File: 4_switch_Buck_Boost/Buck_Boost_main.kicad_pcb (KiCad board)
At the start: 4 copper layers, 96 parts, among them J1 Conn_02x02_Counter_Clockwise, J2 Screw_Terminal_2x5.08, J3 Screw_Terminal_2x2.54, J4 Screw_Terminal_2x5.08, Q101 2N7002K, Q102 NVMFS6H836NLT1G, Q103 BSS83P, Q104 BSC070N10LS5, Q105 BSC070N10LS5, Q106 BSC070N10LS5, Q107 BSC070N10LS5, U1 LT8390EUFD_PBF, U101 LTC4372CMS8-PBF

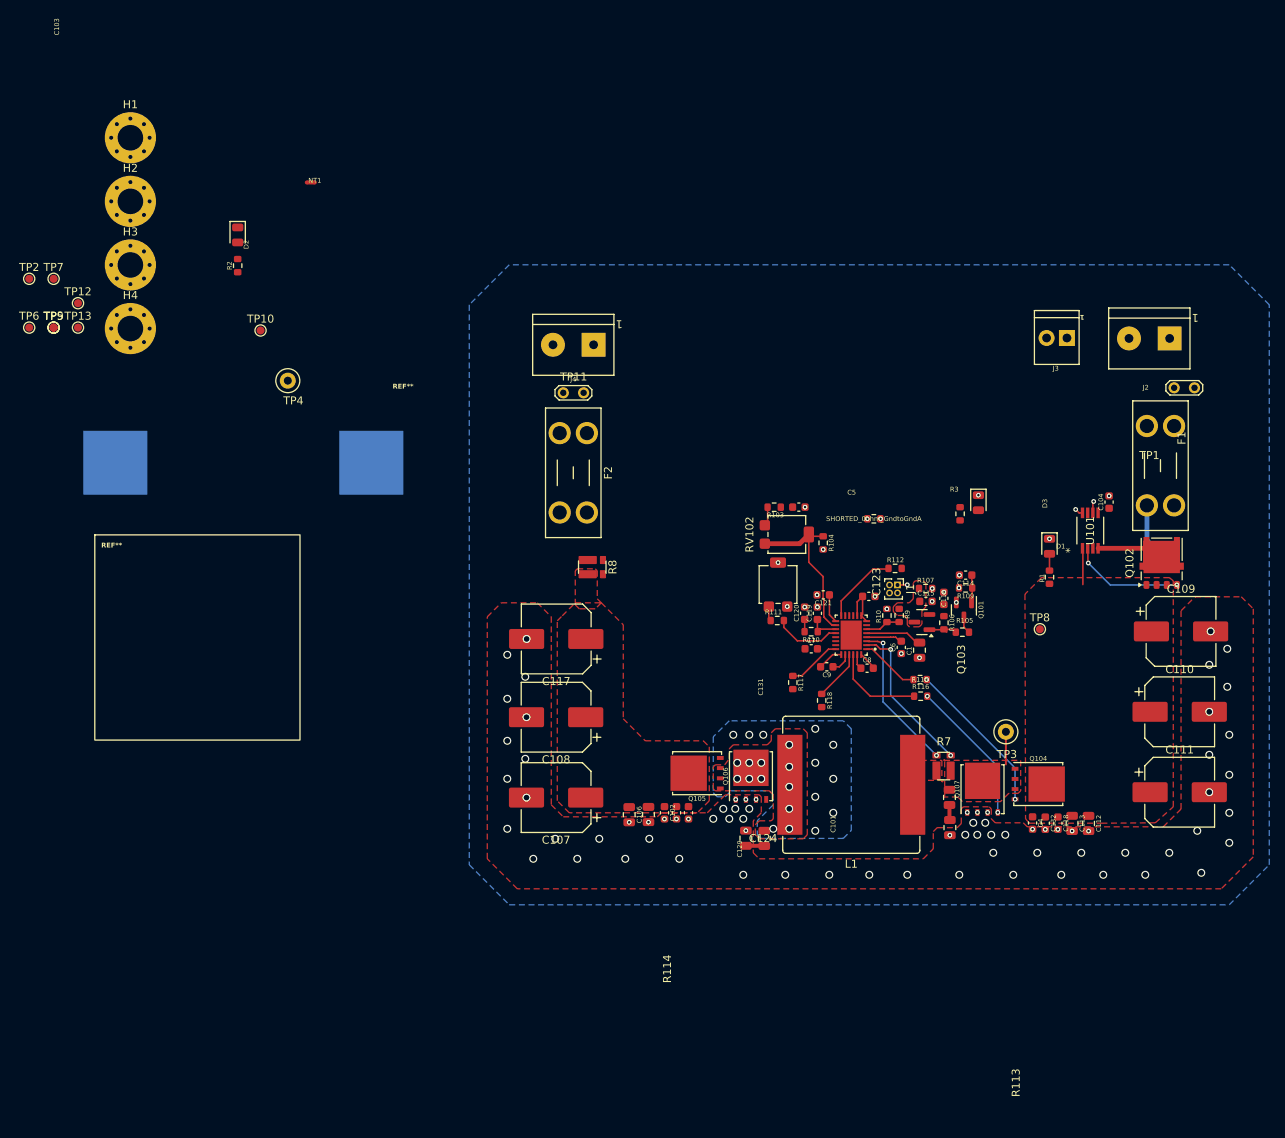
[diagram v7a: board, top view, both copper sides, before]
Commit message: Configured LED, pores, and all test points
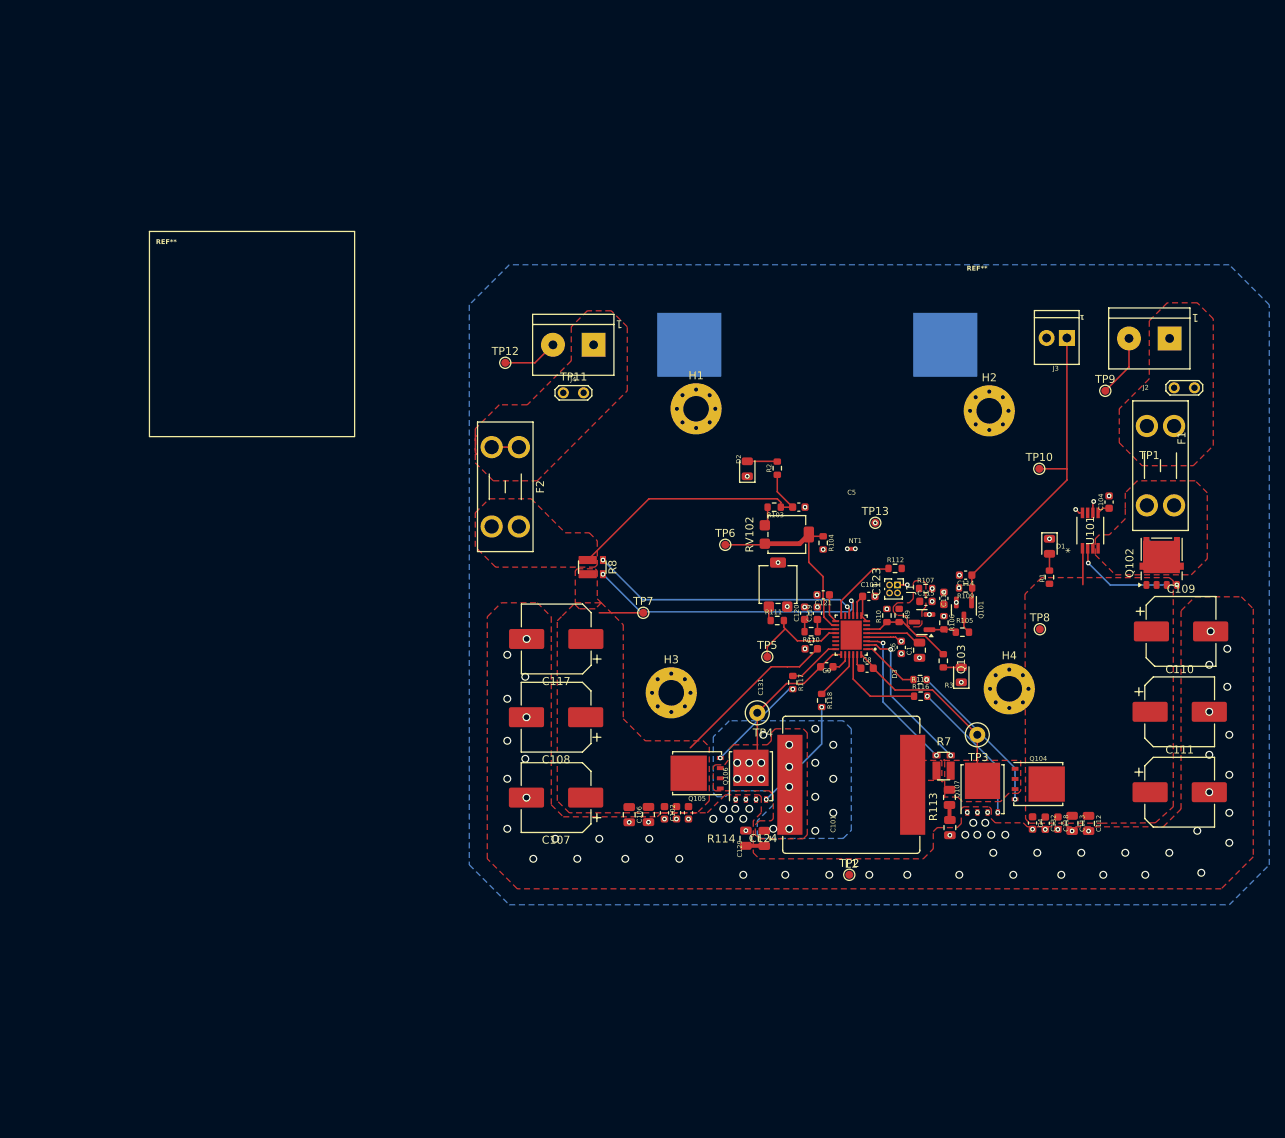
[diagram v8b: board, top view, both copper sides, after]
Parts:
- removed SHORTED_0ohm_GndtoGndA: R_short, rsx_resistors:R_0603_1608Metric
- moved TP9 131.7 mm to (176.0, 71.2)
- moved TP2 126.7 mm to (144.0, 131.8)
- moved H4 118.7 mm to (164.0, 108.5)
- moved H2 110.5 mm to (161.5, 73.8)
- moved TP13 102.6 mm to (147.2, 87.8)
- moved TP10 98.9 mm to (167.8, 81.0)
- moved TP5 98.2 mm to (133.8, 104.5)
- moved TP6 91.1 mm to (128.5, 90.5)
- moved H3 86.2 mm to (121.8, 109.0)
- moved TP7 84.7 mm to (118.2, 99.0)
- moved NT1 81.6 mm to (144.2, 91.0)
- moved H1 78.4 mm to (124.8, 73.5)
- moved F3 73.3 mm to (140.0, 65.5)
- moved R2 72.0 mm to (135.0, 80.9)
- moved TP4 71.9 mm to (132.5, 111.5)
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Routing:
- net ENABLE: track 3.47 -> 41.5 mm
- net ISP: track 0.00 -> 36.2 mm, vias 0 -> 2
- net Vout_FB: track 0.00 -> 34.7 mm
- net ISN: track 0.00 -> 34.2 mm, vias 0 -> 2
- net Vout: track 0.00 -> 26.5 mm
- net SW1: track 2.33 -> 24.8 mm
- net SW2: track 3.21 -> 20.7 mm, vias 22 -> 20
- net GND: track 2.49 -> 17.2 mm, vias 88 -> 92
- net Net-(Q106-G): track 0.00 -> 14.4 mm, vias 0 -> 2
- net Net-(Q105-G): track 0.00 -> 12.6 mm, vias 0 -> 2
- net Net-(Q102-D): track 15.7 -> 4.43 mm
- net EN/UVLO: track 4.43 -> 11.6 mm
- net FB: track 20.9 -> 25.9 mm
- net OUTPUT: track 0.00 -> 4.70 mm
- net Net-(U1-RT): track 8.43 -> 12.9 mm
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- added copper zone on F.Cu, net BAT
- added copper zone on F.Cu, net Net-(Q102-D)
- added copper zone on F.Cu, net OUTPUT
- added copper zone on F.Cu, net Vout_FB
